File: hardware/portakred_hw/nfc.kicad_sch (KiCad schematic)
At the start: 14 parts, among them U1 PN5120A0HN1, Y1 27.12MHz

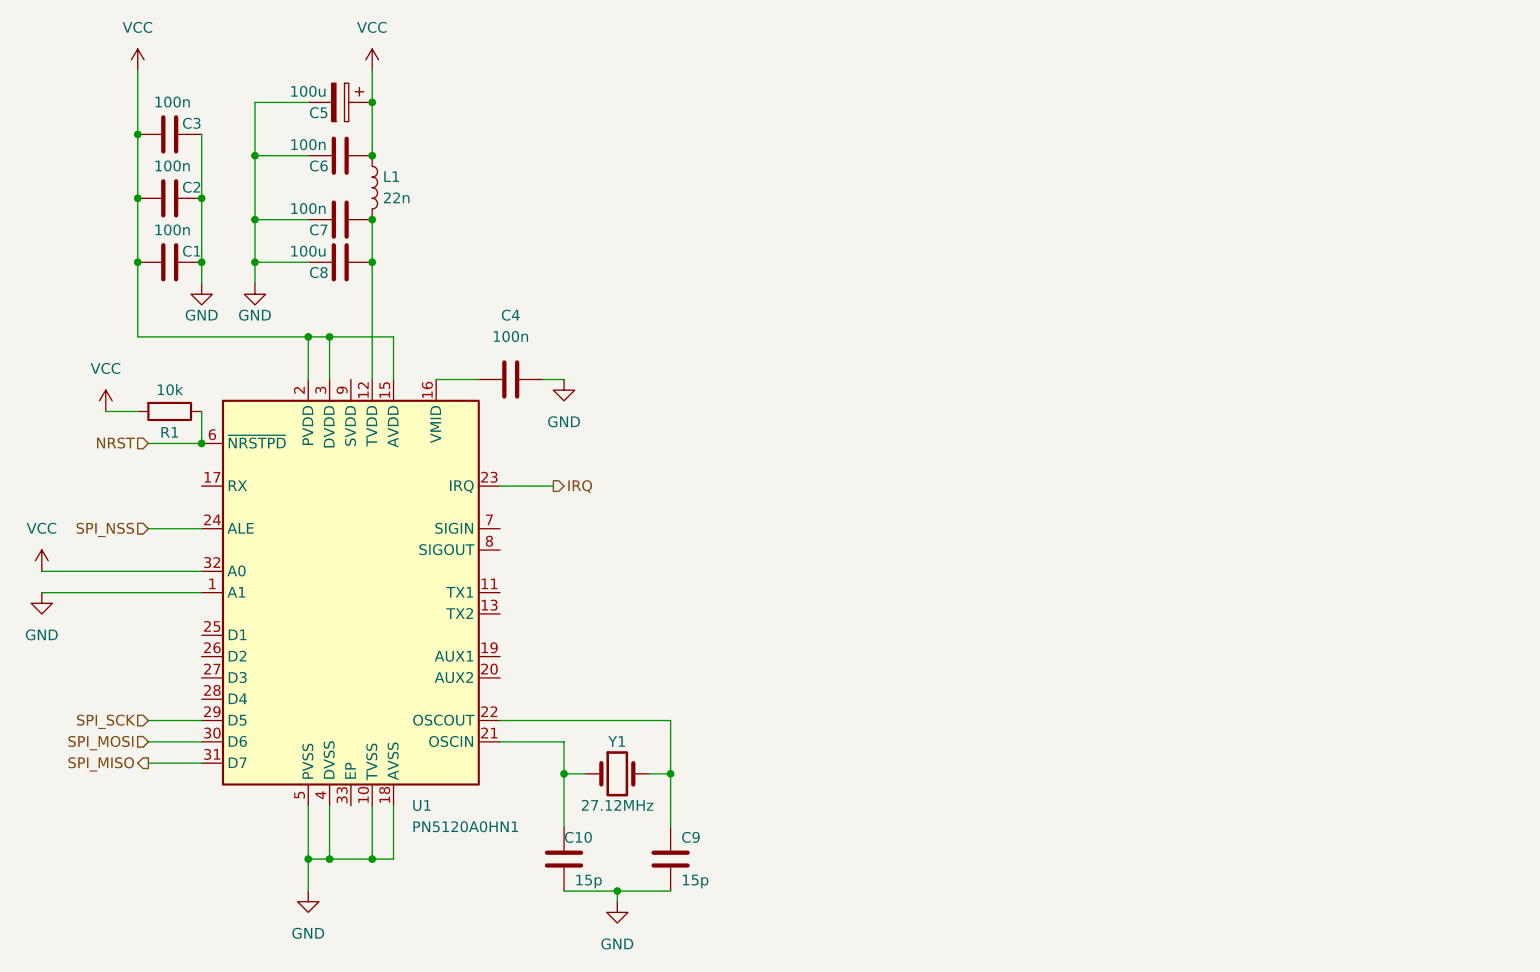
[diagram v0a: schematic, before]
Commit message: Connected peripherals to ESP, Added NFC antenna circuitry, added buzzer
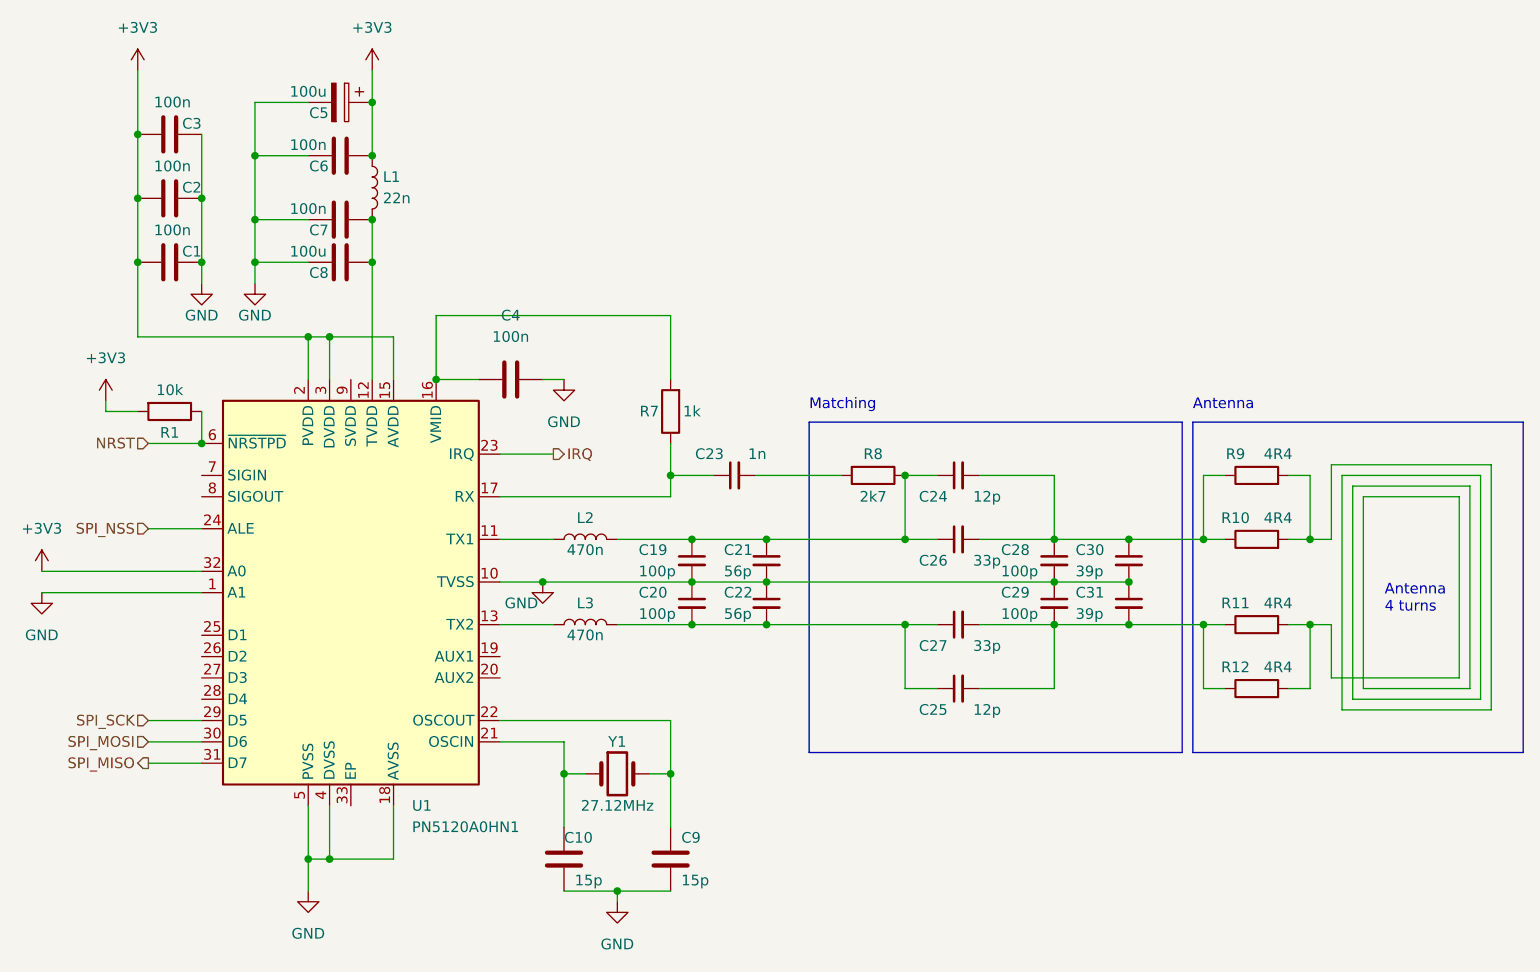
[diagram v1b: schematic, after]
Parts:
- added C19, C20, C28, C29: 100p, symbol Device:C_Small
- added C21, C22: 56p, symbol Device:C_Small
- added C23: 1n, symbol Device:C_Small
- added C24, C25: 12p, symbol Device:C_Small
- added C26, C27: 33p, symbol Device:C_Small
- added C30, C31: 39p, symbol Device:C_Small
- added L2, L3: 470n, symbol Device:L
- added R10, R11, R12, R9: 4R4, symbol Device:R
- added R7: 1k, symbol Device:R
- added R8: 2k7, symbol Device:R
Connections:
- net GND: now also C19.2, C20.1, C21.2, C22.1, C28.2, C29.1, C30.2, C31.1; no longer U1.14 (TVSS)
- net at C4.1, U1.16 (VMID): now also R7.2
- net at U1.11 (TX1): now also L2.1
- net at U1.13 (TX2): now also L3.1
- net at U1.17 (RX): now also C23.1, R7.1
- net VCC renamed +3V3
- new net: C25.2, C27.2, C29.2, C31.2, R11.1, R12.1
- new net: R10.2, R11.2, R12.2, R9.2
- new net: C20.2, C22.2, C25.1, C27.1, L3.2
- new net: C24.2, C26.2, C28.1, C30.1, R10.1, R9.1
- new net: C19.1, C21.1, C24.1, C26.1, L2.2, R8.1
- new net: C23.2, R8.2
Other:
- note added: "Antenna"
- note added: "Antenna 4 turns"
- note added: "Matching"

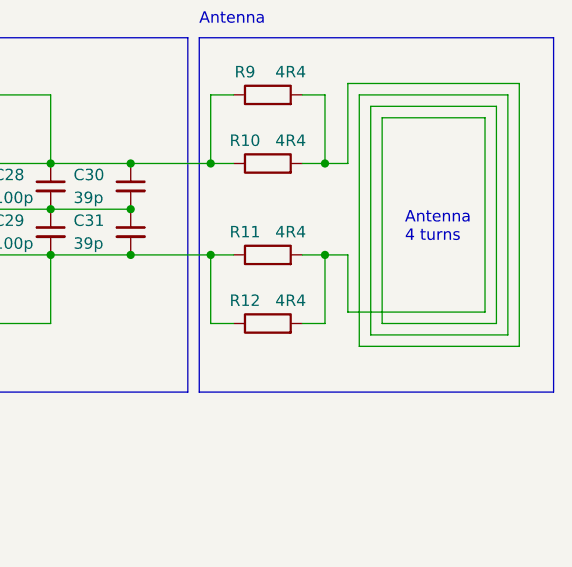
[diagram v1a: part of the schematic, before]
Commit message: Fix buzzer connection, fix keypad diodes and add description, move NFC antenna wire to be pretty :)
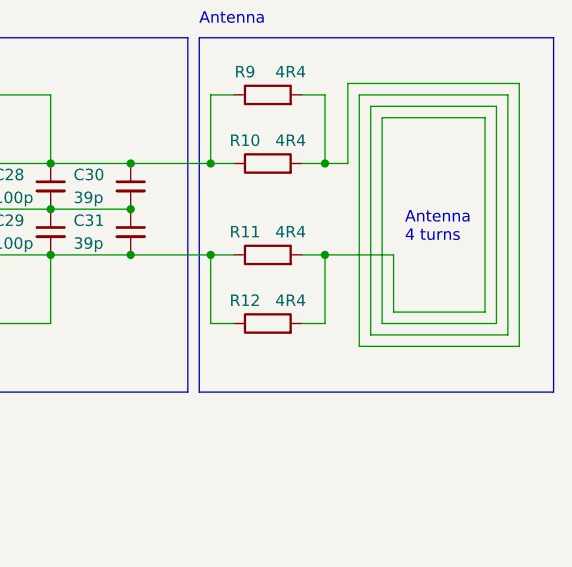
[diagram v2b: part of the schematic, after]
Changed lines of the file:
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@@
     (stroke (width 0) (type default))
   )
-  (wire (pts (xy 257.81 95.25) (xy 255.27 95.25))
+  (wire (pts (xy 262.89 95.25) (xy 255.27 95.25))
     (stroke (width 0) (type default))
   )
@@
     (stroke (width 0) (type default))
   )
-  (wire (pts (xy 257.81 101.6) (xy 257.81 95.25))
+  (wire (pts (xy 262.89 101.6) (xy 262.89 95.25))
     (stroke (width 0) (type default))
   )
@@
     (stroke (width 0) (type default))
   )
-  (wire (pts (xy 273.05 101.6) (xy 257.81 101.6))
+  (wire (pts (xy 273.05 101.6) (xy 262.89 101.6))
     (stroke (width 0) (type default))
   )
